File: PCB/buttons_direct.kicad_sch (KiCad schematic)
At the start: 9 parts

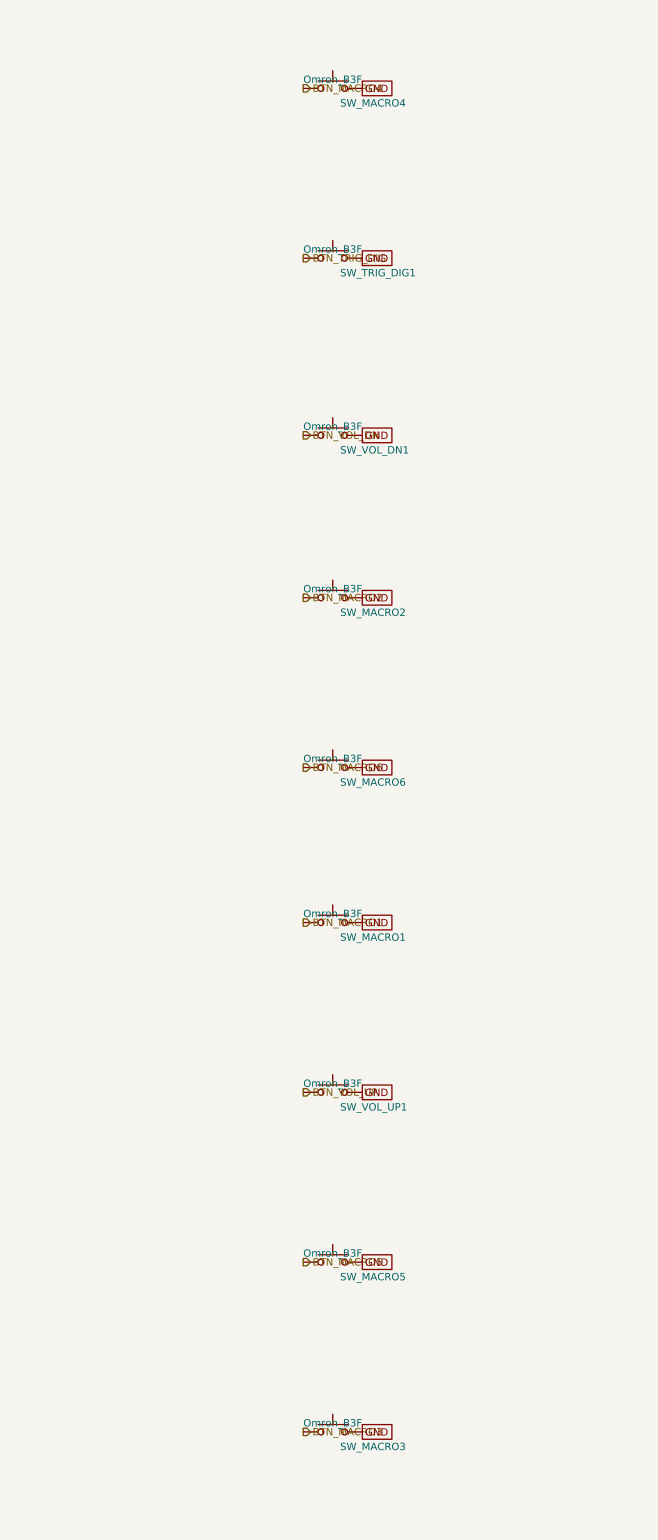
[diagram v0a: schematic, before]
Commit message: Fix footprints and begin layout (#17)
* refactor: updated gulikit footprint

This updates the gulikit thumbstick footprint to be accurate.

* layout: beginning pcb layout

This updates the schematic with a few different footprints while also starts the layout.
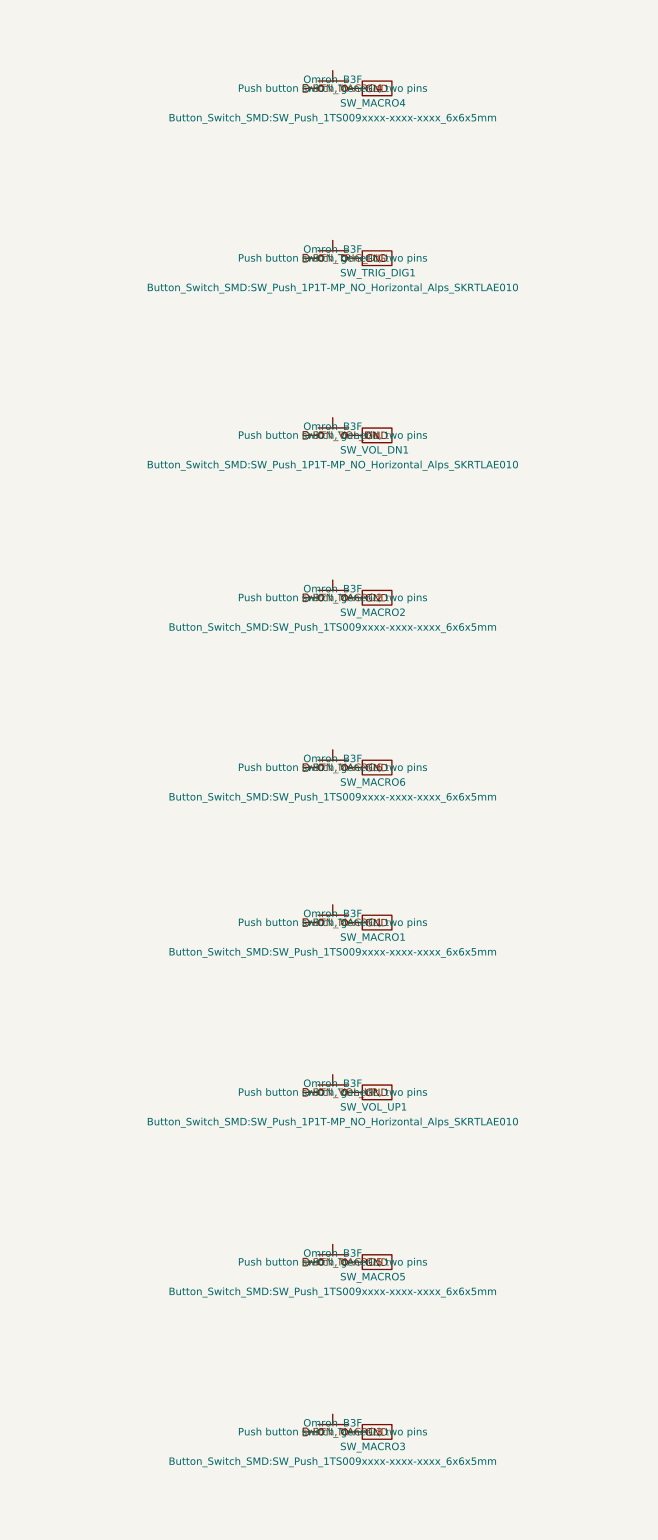
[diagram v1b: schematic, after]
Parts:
- SW_MACRO1, SW_MACRO2, SW_MACRO3, SW_MACRO4, SW_MACRO5, SW_MACRO6: footprint Button_Switch_THT:SW_PUSH_6mm -> Button_Switch_SMD:SW_Push_1TS009xxxx-xxxx-xxxx_6x6x5mm
- SW_TRIG_DIG1, SW_VOL_DN1, SW_VOL_UP1: footprint Button_Switch_THT:SW_PUSH_6mm -> Button_Switch_SMD:SW_Push_1P1T-MP_NO_Horizontal_Alps_SKRTLAE010

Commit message: refactor: swap footprints and add symmetry
This updates the footprints of a couple components to be smaller and closer to what we want. It also adds two buttons to ensure left and right side symmetry.
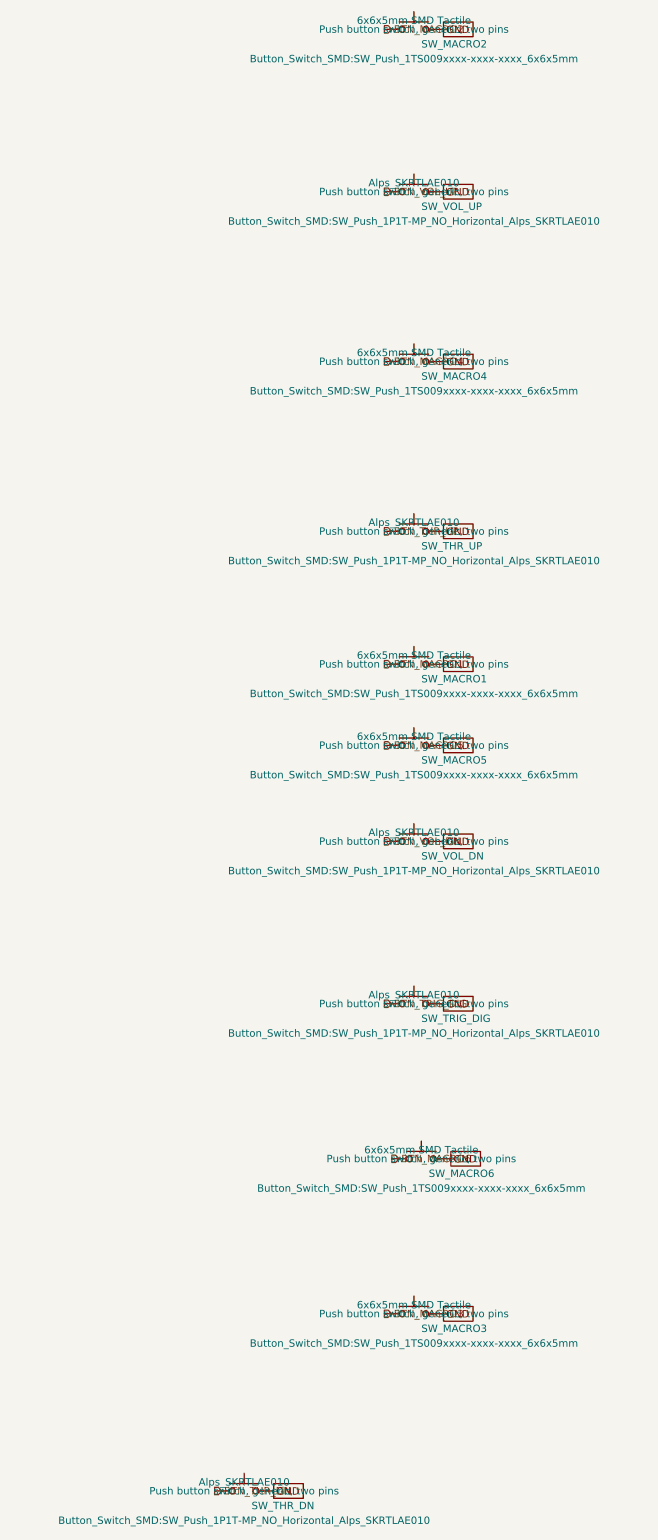
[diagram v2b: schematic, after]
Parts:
- removed SW_TRIG_DIG1, SW_VOL_DN1, SW_VOL_UP1: Omron_B3F, Button_Switch_SMD:SW_Push_1P1T-MP_NO_Horizontal_Alps_SKRTLAE010, symbol Switch:SW_Push
- added SW_THR_DN, SW_THR_UP, SW_TRIG_DIG, SW_VOL_DN, SW_VOL_UP: Alps_SKRTLAE010, Button_Switch_SMD:SW_Push_1P1T-MP_NO_Horizontal_Alps_SKRTLAE010, symbol Switch:SW_Push
- SW_MACRO1, SW_MACRO2, SW_MACRO3, SW_MACRO4, SW_MACRO5, SW_MACRO6: value Omron_B3F -> 6x6x5mm SMD Tactile
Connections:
- net BTN_TRIG_DIG: now also SW_TRIG_DIG.1
- net BTN_VOL_DN: now also SW_VOL_DN.1
- net BTN_VOL_UP: now also SW_VOL_UP.1
- net GND: now also SW_THR_DN.2, SW_THR_UP.2, SW_TRIG_DIG.2, SW_VOL_DN.2, SW_VOL_UP.2
- new net BTN_THR_DN: SW_THR_DN.1
- new net BTN_THR_UP: SW_THR_UP.1

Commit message: layout: everything is on the board
The board edge cuts are down to 100mm x 35mm. All the components have the right footprints and are on the board, but no traces exist yet, and not all circuits are laid out properly yet. Lots of DRC warnings.
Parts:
- removed SW_THR_DN, SW_THR_UP, SW_TRIG_DIG, SW_VOL_DN, SW_VOL_UP: Alps_SKRTLAE010, Button_Switch_SMD:SW_Push_1P1T-MP_NO_Horizontal_Alps_SKRTLAE010, symbol Switch:SW_Push
- added SW_THR_DN1, SW_THR_UP1, SW_TRIG_DIG1, SW_VOL_DN1, SW_VOL_UP1: Alps_SKRTLAE010, Button_Switch_SMD:SW_Push_1P1T-MP_NO_Horizontal_Alps_SKRTLAE010, symbol Switch:SW_Push
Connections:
- net BTN_THR_DN: now also SW_THR_DN1.1
- net BTN_THR_UP: now also SW_THR_UP1.1
- net BTN_TRIG_DIG: now also SW_TRIG_DIG1.1
- net BTN_VOL_DN: now also SW_VOL_DN1.1
- net BTN_VOL_UP: now also SW_VOL_UP1.1
- net GND: now also SW_THR_DN1.2, SW_THR_UP1.2, SW_TRIG_DIG1.2, SW_VOL_DN1.2, SW_VOL_UP1.2

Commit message: task: part number populated (#26)
kicad-happy run part 2 - MPN numbers populated
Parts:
- SW_MACRO1, SW_MACRO2, SW_MACRO3, SW_MACRO4, SW_MACRO5, SW_MACRO6: MF (none) -> Hongyuan Precision; Manufacturer_Part_Number (none) -> 1TS009A-1800-5000-CT
- SW_THR_DN1, SW_THR_UP1, SW_TRIG_DIG1, SW_VOL_DN1, SW_VOL_UP1: MF (none) -> Alps Alpine; Manufacturer_Part_Number (none) -> SKRTLAE010
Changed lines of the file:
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@@
+			)
+		)
+		(property "MF" "Hongyuan Precision" (at 0 0 0)
+			(effects
+				(font
+					(size 1.27 1.27)
+				)
+				(hide yes)
+			)
+		)
+		(property "Manufacturer_Part_Number" "1TS009A-1800-5000-CT" (at 0 0 0)
+			(effects
+				(font
+					(size 1.27 1.27)
+				)
+				(hide yes)
 			)
 		)
@@
 			)
 		)
+		(property "MF" "Hongyuan Precision" (at 0 0 0)
+			(effects
+				(font
+					(size 1.27 1.27)
+				)
+				(hide yes)
+			)
+		)
+		(property "Manufacturer_Part_Number" "1TS009A-1800-5000-CT" (at 0 0 0)
+			(effects
+				(font
+					(size 1.27 1.27)
+				)
+				(hide yes)
+			)
+		)
 		(pin "1"
 		)
@@
 			)
 		)
+		(property "MF" "Hongyuan Precision" (at 0 0 0)
+			(effects
+				(font
+					(size 1.27 1.27)
+				)
+				(hide yes)
+			)
+		)
+		(property "Manufacturer_Part_Number" "1TS009A-1800-5000-CT" (at 0 0 0)
+			(effects
+				(font
+					(size 1.27 1.27)
+				)
+				(hide yes)
+			)
+		)
 		(pin "1"
 		)
@@
 			)
 		)
+		(property "MF" "Alps Alpine" (at 0 0 0)
+			(effects
+				(font
+					(size 1.27 1.27)
+				)
+				(hide yes)
+			)
+		)
+		(property "Manufacturer_Part_Number" "SKRTLAE010" (at 0 0 0)
+			(effects
+				(font
+					(size 1.27 1.27)
+				)
+				(hide yes)
+			)
+		)
 		(pin "1"
 		)
@@
 			)
 		)
+		(property "MF" "Alps Alpine" (at 0 0 0)
+			(effects
+				(font
+					(size 1.27 1.27)
+				)
+				(hide yes)
+			)
+		)
+		(property "Manufacturer_Part_Number" "SKRTLAE010" (at 0 0 0)
+			(effects
+				(font
+					(size 1.27 1.27)
+				)
+				(hide yes)
+			)
+		)
 		(pin "1"
 		)
@@
 			)
 		)
+		(property "MF" "Hongyuan Precision" (at 0 0 0)
+			(effects
+				(font
+					(size 1.27 1.27)
+				)
+				(hide yes)
+			)
+		)
+		(property "Manufacturer_Part_Number" "1TS009A-1800-5000-CT" (at 0 0 0)
+			(effects
+				(font
+					(size 1.27 1.27)
+				)
+				(hide yes)
+			)
+		)
 		(pin "1"
 		)
@@
 			)
 		)
+		(property "MF" "Alps Alpine" (at 0 0 0)
+			(effects
+				(font
+					(size 1.27 1.27)
+				)
+				(hide yes)
+			)
+		)
+		(property "Manufacturer_Part_Number" "SKRTLAE010" (at 0 0 0)
+			(effects
+				(font
+					(size 1.27 1.27)
+				)
+				(hide yes)
+			)
+		)
 		(pin "1"
 		)
@@
 			)
 		)
+		(property "MF" "Hongyuan Precision" (at 0 0 0)
+			(effects
+				(font
+					(size 1.27 1.27)
+				)
+				(hide yes)
+			)
+		)
+		(property "Manufacturer_Part_Number" "1TS009A-1800-5000-CT" (at 0 0 0)
+			(effects
+				(font
+					(size 1.27 1.27)
+				)
+				(hide yes)
+			)
+		)
 		(pin "1"
 		)
@@
 			)
 		)
+		(property "MF" "Alps Alpine" (at 0 0 0)
+			(effects
+				(font
+					(size 1.27 1.27)
+				)
+				(hide yes)
+			)
+		)
+		(property "Manufacturer_Part_Number" "SKRTLAE010" (at 0 0 0)
+			(effects
+				(font
+					(size 1.27 1.27)
+				)
+				(hide yes)
+			)
+		)
 		(pin "1"
 		)
@@
 			)
 		)
+		(property "MF" "Alps Alpine" (at 0 0 0)
+			(effects
+				(font
+					(size 1.27 1.27)
+				)
+				(hide yes)
+			)
+		)
+		(property "Manufacturer_Part_Number" "SKRTLAE010" (at 0 0 0)
+			(effects
+				(font
+					(size 1.27 1.27)
+				)
+				(hide yes)
+			)
+		)
 		(pin "1"
 		)
@@
 			)
 		)
+		(property "MF" "Hongyuan Precision" (at 0 0 0)
+			(effects
+				(font
+					(size 1.27 1.27)
+				)
+				(hide yes)
+			)
+		)
+		(property "Manufacturer_Part_Number" "1TS009A-1800-5000-CT" (at 0 0 0)
+			(effects
+				(font
+					(size 1.27 1.27)
+				)
+				(hide yes)
+			)
+		)
